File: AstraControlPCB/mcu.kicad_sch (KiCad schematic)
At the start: 10 parts, among them U1 ESP32-S3-WROOM-1U-N8

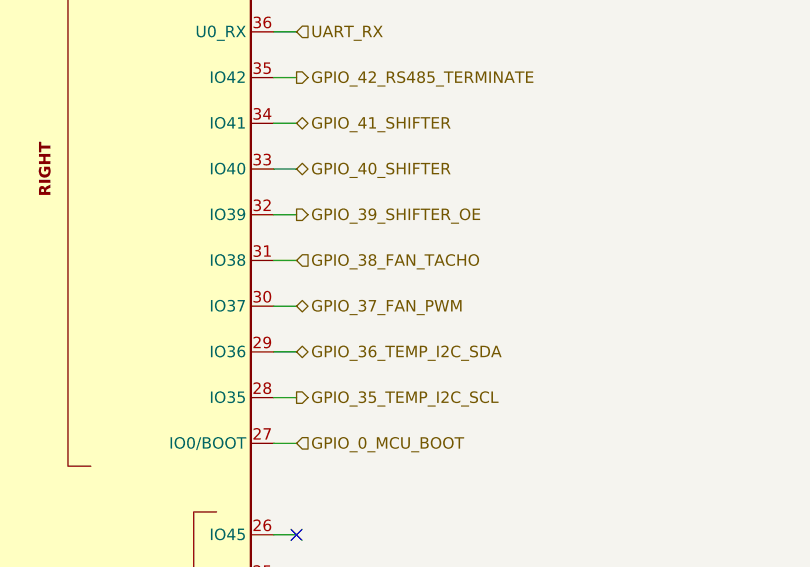
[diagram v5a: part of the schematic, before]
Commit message: Update fan to rpi style pinout, minor cosmetic fixes
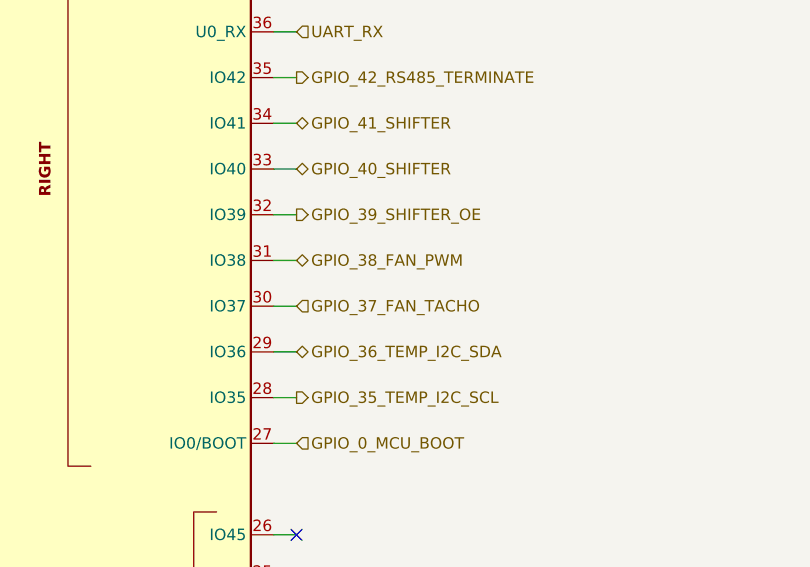
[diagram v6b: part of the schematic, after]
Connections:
- net GPIO_37_FAN_PWM renamed GPIO_37_FAN_TACHO
- net GPIO_38_FAN_TACHO renamed GPIO_38_FAN_PWM
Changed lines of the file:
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@@
+		)
+	)
+	(hierarchical_label "GPIO_37_FAN_TACHO"
+		(shape input)
+		(at 185.42 91.44 0)
+		(fields_autoplaced yes)
+		(effects
+			(font
+				(size 1.27 1.27)
+			)
+			(justify left)
+		)
+	)
+	(hierarchical_label "GPIO_38_FAN_PWM"
+		(shape bidirectional)
+		(at 185.42 86.36 0)
+		(fields_autoplaced yes)
+		(effects
+			(font
+				(size 1.27 1.27)
+			)
+			(justify left)
 		)
 	)
@@
 		)
 	)
-	(hierarchical_label "GPIO_37_FAN_PWM"
-		(shape bidirectional)
-		(at 185.42 91.44 0)
-		(fields_autoplaced yes)
-		(effects
-			(font
-				(size 1.27 1.27)
-			)
-			(justify left)
-		)
-	)
 	(hierarchical_label "GPIO_4_RS485_TX"
 		(shape output)
@@
 		)
 	)
-	(hierarchical_label "GPIO_38_FAN_TACHO"
-		(shape input)
-		(at 185.42 86.36 0)
-		(fields_autoplaced yes)
-		(effects
-			(font
-				(size 1.27 1.27)
-			)
-			(justify left)
-		)
-	)

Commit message: Update revision and add year to silkscreen
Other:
- title: AstraControl - MCU -> AstraControl - Root
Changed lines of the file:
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@@
 	(paper "A4")
 	(title_block
-		(title "AstraControl - MCU")
+		(title "AstraControl - Root")
 		(date "2024-08-26")
-		(rev "A")
+		(rev "B")
 		(company "LiveAstra Technologies")
 	)

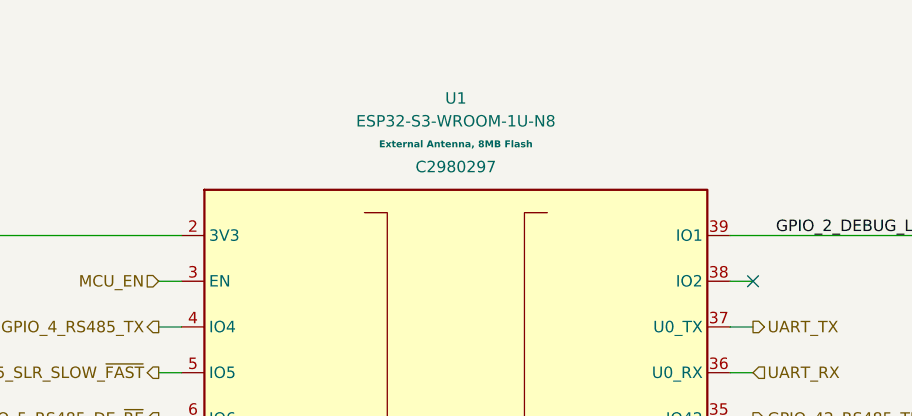
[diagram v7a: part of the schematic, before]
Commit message: Swap to ESP 32 S3 N16 for availability
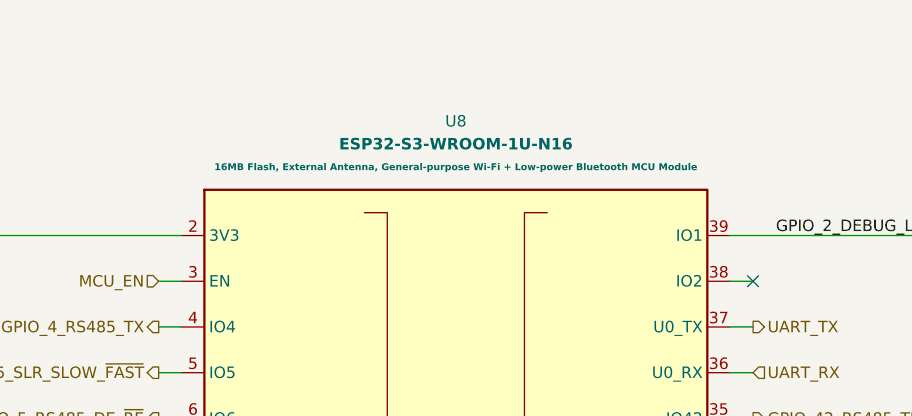
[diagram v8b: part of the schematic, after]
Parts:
- removed U1: ESP32-S3-WROOM-1U-N8, LiveAstra:WIRELM-SMD_ESP32-S3-WROOM-1U, symbol LiveAstra:ESP32-S3-WROOM-1U-N8
- added U8: ESP32-S3-WROOM-1U-N16, LiveAstra:WIRELM-SMD_ESP32-S3-WROOM-1U, symbol LiveAstra:U_ESP32-S3-WROOM-1U-N16
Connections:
- net 3V3: now also U8.2 (3V3)
- net GND: now also U8.1 (GND), U8.40 (GND), U8.41 (EP)
- net GPIO_0_MCU_BOOT: now also U8.27 (IO0/BOOT)
- net GPIO_10_SCREEN_I2C_SDA: now also U8.18 (IO10)
- net GPIO_12_STATUS_LED: now also U8.20 (IO12)
- net GPIO_13_BUTTON: now also U8.21 (IO13)
- net GPIO_14_I2S_LR: now also U8.22 (IO14)
- net GPIO_15_PWM_CH4: now also U8.8 (IO15)
- net GPIO_16_PWM_CH3: now also U8.9 (IO16)
- net GPIO_17_PWM_CH2: now also U8.10 (IO17)
- net GPIO_18_PWM_CH1: now also U8.11 (IO18)
- net GPIO_21_I2S_WS: now also U8.23 (IO21)
- net GPIO_2_DEBUG_LED: now also U8.39 (IO1)
- net GPIO_35_TEMP_I2C_SCL: now also U8.28 (IO35)
- net GPIO_36_TEMP_I2C_SDA: now also U8.29 (IO36)
- net GPIO_37_FAN_TACHO: now also U8.30 (IO37)
- net GPIO_38_FAN_PWM: now also U8.31 (IO38)
- net GPIO_39_SHIFTER_OE: now also U8.32 (IO39)
- net GPIO_40_SHIFTER: now also U8.33 (IO40)
- net GPIO_41_SHIFTER: now also U8.34 (IO41)
- net GPIO_42_RS485_TERMINATE: now also U8.35 (IO42)
- net GPIO_47_I2S_SCK: now also U8.24 (IO47)
- net GPIO_48_I2S_SD: now also U8.25 (IO48)
- net GPIO_4_RS485_TX: now also U8.4 (IO4)
- net GPIO_5_RS485_DE_~{RE}: now also U8.6 (IO6)
- net GPIO_6_RS485_SLR_SLOW_~{FAST}: now also U8.5 (IO5)
- net GPIO_7_RS485_RX: now also U8.7 (IO7)
- net GPIO_8: now also U8.12 (IO8)
- net GPIO_9_SCREEN_I2C_SCL: now also U8.17 (IO9)
- net IO_3_IC: now also U8.15 (IO3)
- net MCU_EN: now also U8.3 (EN)
- net UART_RX: now also U8.36 (U0_RX)
- net UART_TX: now also U8.37 (U0_TX)
- net USB_D+: now also U8.14 (IO20/USB_D+)
- net USB_D-: now also U8.13 (IO19/USB_D-)
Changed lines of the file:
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@@
 	)
 	(symbol
-		(lib_id "LiveAstra:ESP32-S3-WROOM-1U-N8")
+		(lib_id "LiveAstra:U_ESP32-S3-WROOM-1U-N16")
 		(at 152.4 93.98 0)
 		(unit 1)
@@
 		(dnp no)
 		(fields_autoplaced yes)
-		(property "Reference" "U1"
-			(at 152.4 30.48 0)
-			(effects
-				(font
-					(size 1.27 1.27)
-				)
-			)
-		)
-		(property "Value" "ESP32-S3-WROOM-1U-N8"
+		(property "Reference" "U8"
 			(at 152.4 33.02 0)
 			(effects
@@
 			)
 		)
+		(property "Value" "ESP32-S3-WROOM-1U-N16"
+			(at 152.4 35.56 0)
+			(effects
+				(font
+					(size 1.27 1.27)
+					(bold yes)
+				)
+			)
+		)
 		(property "Footprint" "LiveAstra:WIRELM-SMD_ESP32-S3-WROOM-1U"
-			(at 152.4 171.45 0)
+			(at 152.4 165.1 0)
 			(effects
 				(font
@@
 			)
 		)
-		(property "Datasheet" "https://www.lcsc.com/product-detail/WiFi-Modules_Espressif-Systems-ESP32-S3-WROOM-1U-N8_C2980297.html"
-			(at 152.4 161.29 0)
+		(property "Datasheet" "https://www.lcsc.com/product-detail/WiFi-Modules_Espressif-Systems-ESP32-S3-WROOM-1U-N16_C2980298.html"
+			(at 152.4 185.42 0)
 			(effects
 				(font
@@
 			)
 		)
-		(property "Description" "RF Module, ESP32-S3 SoC, Wi-Fi 802.11b/g/n, Bluetooth, BLE, 32-bit, 3.3V, onboard antenna, SMD"
-			(at 153.67 166.37 0)
+		(property "Description" "SMD,18x19.2mm WiFi Modules ROHS"
+			(at 152.4 180.34 0)
 			(effects
 				(font
@@
 			)
 		)
-		(property "Extra Values" "External Antenna, 8MB Flash"
-			(at 152.4 35.56 0)
+		(property "LCSC Part" "C2980298"
+			(at 152.4 170.18 0)
+			(effects
+				(font
+					(size 1.27 1.27)
+				)
+				(hide yes)
+			)
+		)
+		(property "Extra Values" "16MB Flash, External Antenna, General-purpose Wi-Fi + Low-power Bluetooth MCU Module"
+			(at 152.4 38.1 0)
 			(effects
 				(font
@@
 			)
 		)
-		(property "LCSC Part" "C2980297"
-			(at 152.4 38.1 0)
-			(effects
-				(font
-					(size 1.27 1.27)
-				)
-			)
-		)
 		(property "MFN" "Espressif Systems"
-			(at 152.4 176.53 0)
+			(at 152.4 175.26 0)
 			(effects
 				(font
@@
 			)
 		)
-		(property "MPN" "ESP32-S3-WROOM-1U-N8"
-			(at 152.4 176.53 0)
+		(property "MPN" "ESP32-S3-WROOM-1U-N16"
+			(at 152.4 190.5 0)
 			(effects
 				(font
@@
 			)
 		)
-		(pin "11"
+		(pin "21"
 		)
-		(pin "12"
+		(pin "22"
+		)
+		(pin "4"
+		)
+		(pin "1"
 		)
 		(pin "13"
-		)
-		(pin "23"
-		)
-		(pin "24"
-		)
-		(pin "25"
-		)
-		(pin "26"
-		)
-		(pin "27"
 		)
 		(pin "5"
@@
 		(pin "6"
 		)
-		(pin "7"
+		(pin "14"
 		)
-		(pin "8"
+		(pin "40"
 		)
-		(pin "9"
+		(pin "41"
+		)
+		(pin "17"
+		)
+		(pin "29"
+		)
+		(pin "3"
 		)
 		(pin "30"
@@
 		(pin "33"
 		)
-		(pin "34"
+		(pin "23"
 		)
-		(pin "35"
+		(pin "24"
+		)
+		(pin "18"
+		)
+		(pin "19"
+		)
+		(pin "15"
 		)
 		(pin "36"
@@
 		(pin "37"
 		)
+		(pin "25"
+		)
+		(pin "26"
+		)
+		(pin "27"
+		)
+		(pin "28"
+		)
 		(pin "38"
 		)
 		(pin "39"
-		)
-		(pin "4"
-		)
-		(pin "40"
-		)
-		(pin "41"
-		)
-		(pin "14"
-		)
-		(pin "15"
-		)
-		(pin "16"
-		)
-		(pin "17"
-		)
-		(pin "28"
-		)
-		(pin "29"
-		)
-		(pin "3"
-		)
-		(pin "18"
-		)
-		(pin "19"
 		)
 		(pin "2"
@@
 		(pin "20"
 		)
-		(pin "21"
+		(pin "7"
 		)
-		(pin "22"
-		)
-		(pin "1"
+		(pin "8"
 		)
 		(pin "10"
 		)
+		(pin "16"
+		)
+		(pin "9"
+		)
+		(pin "12"
+		)
+		(pin "34"
+		)
+		(pin "35"
+		)
+		(pin "11"
+		)
 		(instances
-			(project "AstraControl"
+			(project ""
 				(path "/9a751838-dce8-4d69-8a02-736625ac74e7/0db21d8e-3390-4d67-877f-0e5d98e37848/3087dd4a-2a8a-4df4-b1d8-8d4a2b3256a2"
-					(reference "U1")
+					(reference "U8")
 					(unit 1)
 				)
